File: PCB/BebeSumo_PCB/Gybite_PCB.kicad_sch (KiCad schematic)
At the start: 17 parts, among them J1 Pulsador, J10 JSUMO, J11 Sharps, J12 Conector Batería, J2 Motor 1, J3 HC-SR04, J4 Motor 2, J5 QRE1113, J6 QRE1113, J7 Arduino_Nano_Header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

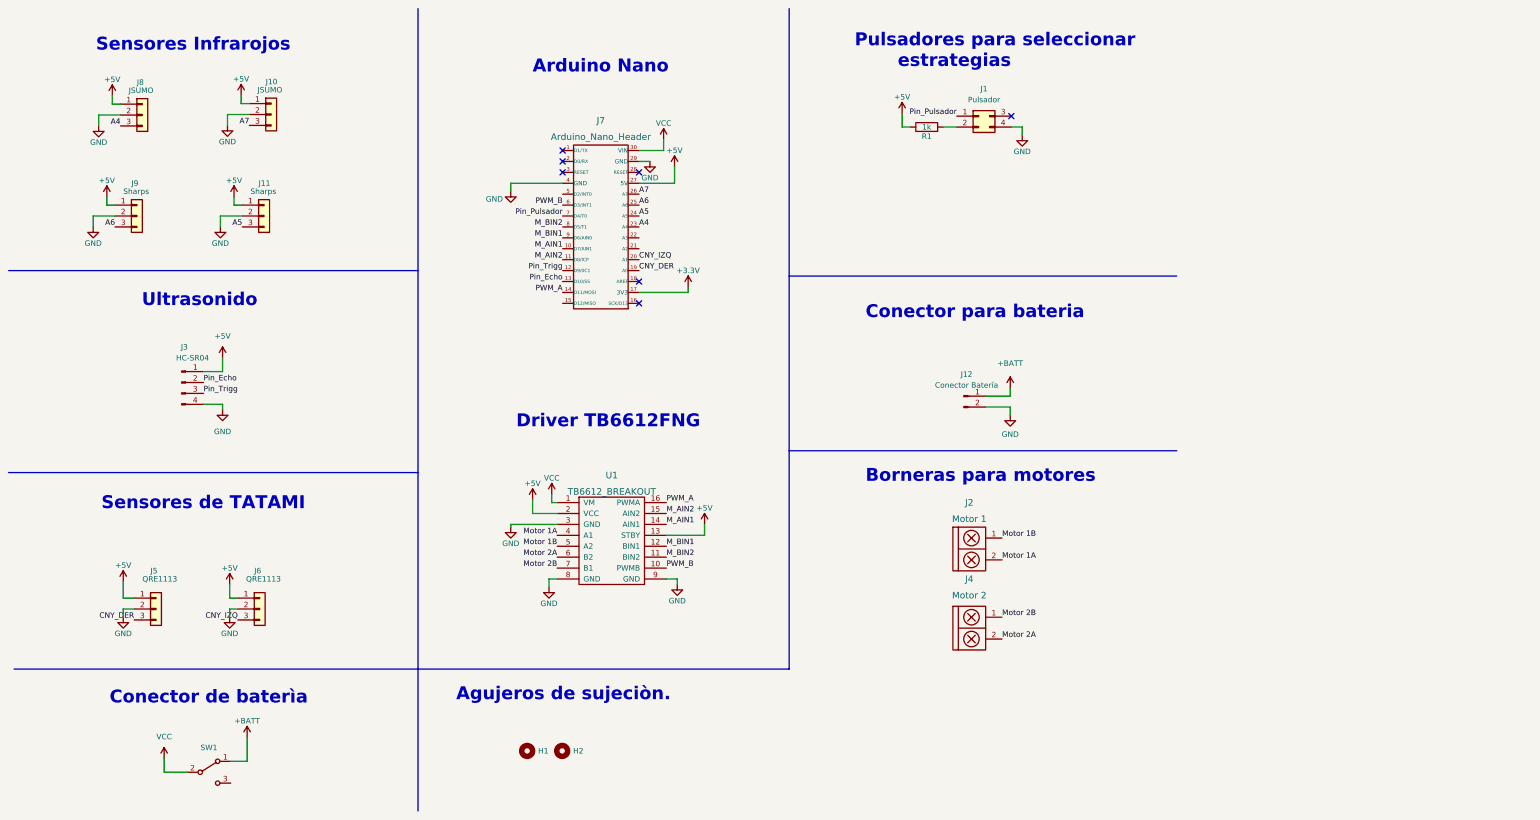
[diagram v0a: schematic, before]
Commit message: Rediseño de la placa, ahora tiene un dip y la huella para el nuevo interruptor de corriente.
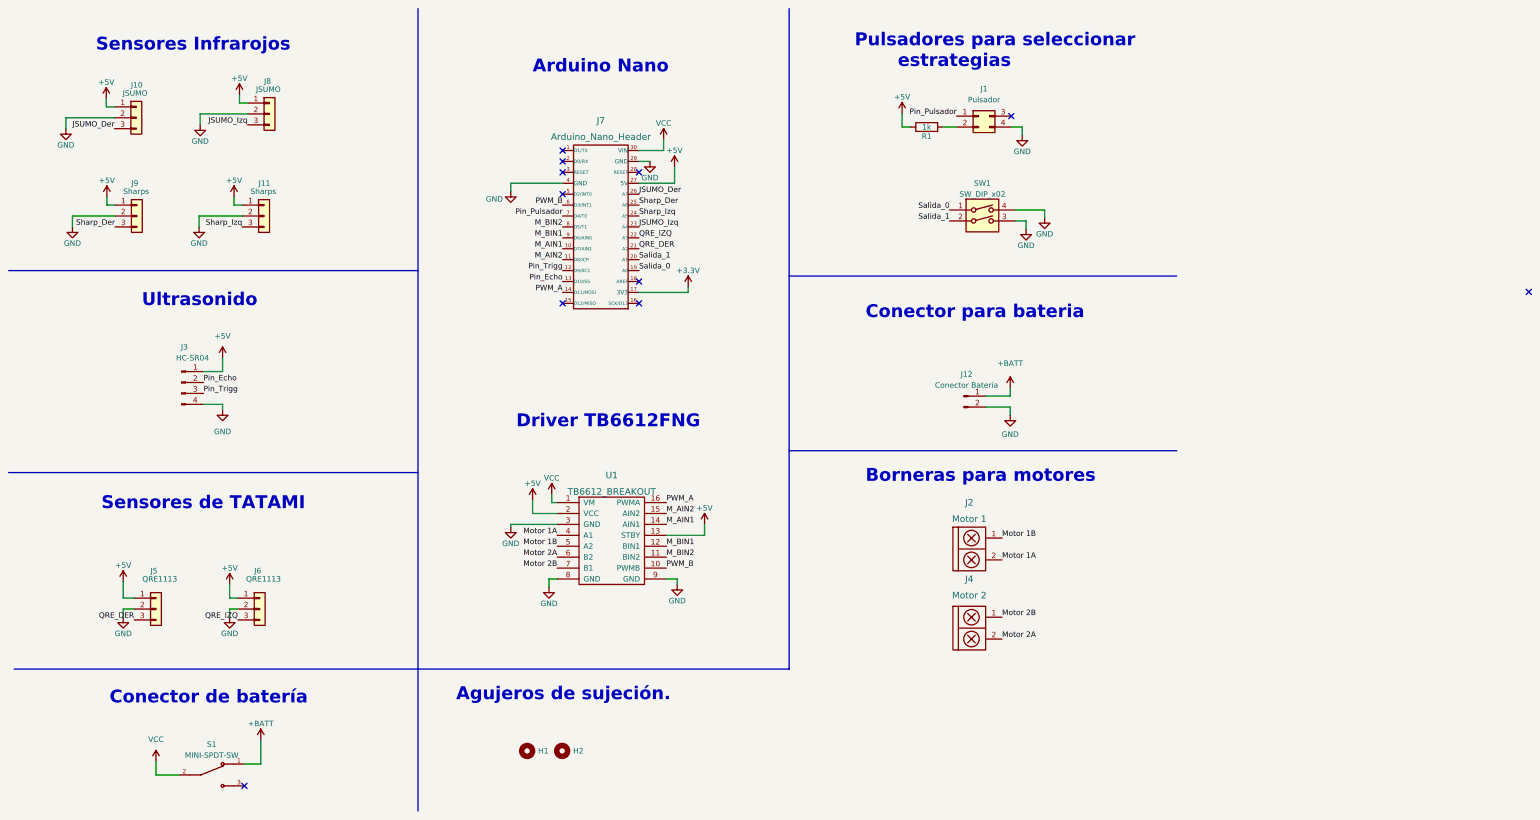
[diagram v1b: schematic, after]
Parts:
- removed SW1: SW_SPDT, EESTN5:SW_SPDT_TH_Vertical, symbol EESTN5:SW_SPDT
- added S1: MINI-SPDT-SW, Switch.prety:Switch_SS12F44_123, symbol MINI-SPDT-SW:MINI-SPDT-SW
- added SW1: SW_DIP_x02, Button_Switch_THT:SW_DIP_SPSTx02_Slide_9.78x7.26mm_W7.62mm_P2.54mm, symbol Switch:SW_DIP_x02
- H1, H2: footprint EESTN5:hole_3mm -> EESTN5:hole_2mm
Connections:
- net +BATT: now also S1.1
- net GND: now also SW1.3, SW1.4
- net VCC: now also S1.2
- net QRE_DER: now reaches J7.21 (A2)
- net QRE_DER: now also J5.3 (Pin_3)
- net QRE_IZQ: now reaches J7.22 (A3)
- net QRE_IZQ: now also J6.3 (Pin_3)
- net A4 renamed JSUMO_Izq
- net A5 renamed Sharp_Izq
- net A6 renamed Sharp_Der
- net A7 renamed JSUMO_Der
- net CNY_DER renamed Salida_0
- net Salida_0: now also SW1.1; no longer J5.3 (Pin_3)
- net CNY_IZQ renamed Salida_1
- net Salida_1: now also SW1.2; no longer J6.3 (Pin_3)
- no-connect marks 7 -> 11
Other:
- note added: "Agujeros de sujeción."
- note added: "Conector de batería"
- note removed: "Agujeros de sujeciòn."
- note removed: "Conector de baterìa"
- moved on the sheet: J10, J8
